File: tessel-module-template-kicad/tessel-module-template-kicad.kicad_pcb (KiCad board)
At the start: 2 copper layers, 0 parts

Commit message: added board outline and guides (we like our modules to be 1.1" high and (1+k*0.25)" long)
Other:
- board outline added: 25.4 x 27.9 mm
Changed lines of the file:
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@@
     (area 0 0 0 0)
     (thickness 1.6)
-    (drawings 0)
+    (drawings 14)
     (tracks 0)
     (zones 0)
@@
     (uvia_drill 0.1)
   )
+  (gr_line (start 171.45 127) (end 171.45 128.27) (layer Dwgs.User) (width 0.2))
+  (gr_line (start 158.75 127) (end 158.75 128.27) (layer Dwgs.User) (width 0.2))
+  (gr_line (start 152.4 127) (end 152.4 128.27) (layer Dwgs.User) (width 0.2))
+  (gr_line (start 165.1 127) (end 165.1 128.27) (layer Dwgs.User) (width 0.2))
+  (gr_line (start 146.05 127) (end 146.05 128.27) (layer Dwgs.User) (width 0.2))
+  (gr_line (start 139.7 127) (end 139.7 128.27) (layer Dwgs.User) (width 0.2))
+  (gr_line (start 133.35 127) (end 133.35 128.27) (layer Dwgs.User) (width 0.2))
+  (gr_line (start 127 127) (end 127 128.27) (layer Dwgs.User) (width 0.2))
+  (gr_arc (start 124.46 101.6) (end 124.46 99.06) (angle 90) (layer Edge.Cuts) (width 0.15))
+  (gr_arc (start 124.46 124.46) (end 127 124.46) (angle 90) (layer Edge.Cuts) (width 0.15))
+  (gr_line (start 124.46 127) (end 101.6 127) (layer Edge.Cuts) (width 0.15))
+  (gr_line (start 127 101.6) (end 127 124.46) (layer Edge.Cuts) (width 0.15))
+  (gr_line (start 101.6 99.06) (end 124.46 99.06) (layer Edge.Cuts) (width 0.15))
+  (gr_line (start 101.6 127) (end 101.6 99.06) (layer Edge.Cuts) (width 0.15))
 )

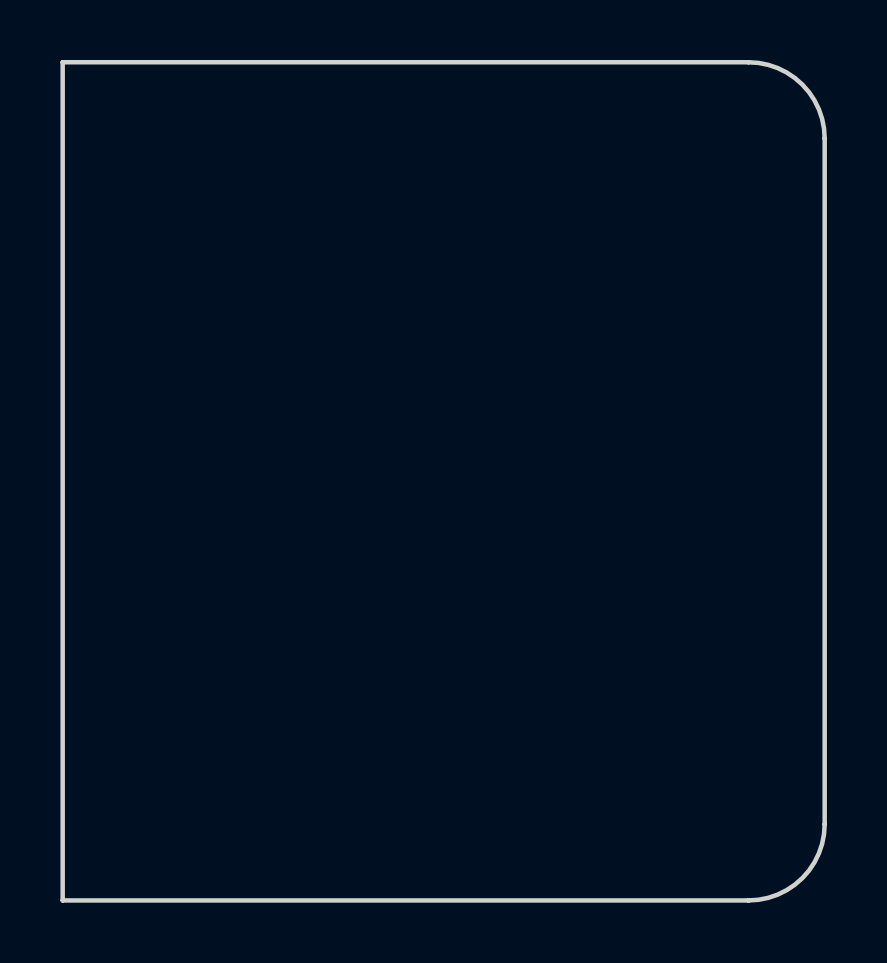
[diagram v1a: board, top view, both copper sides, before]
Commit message: read the netlist and placed the module header (centered on the vertical axis and in 75 mils on the horizontal axis). resized header refdes to 0.7mm text with 0.07mm width.
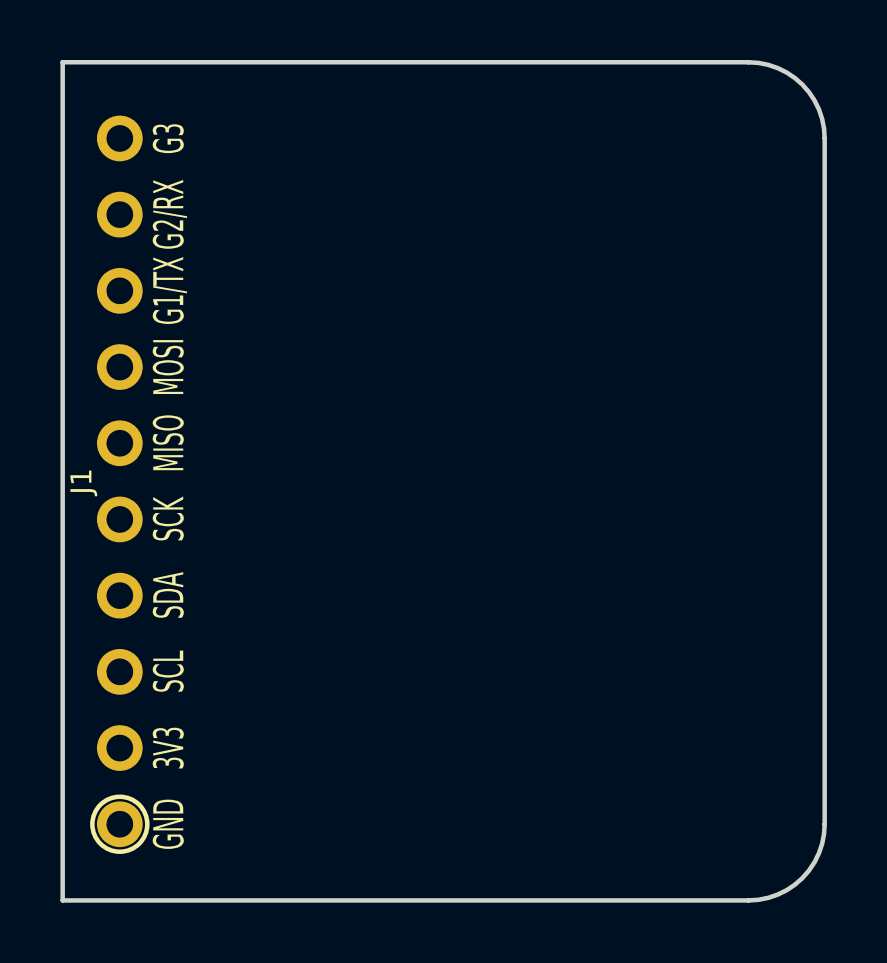
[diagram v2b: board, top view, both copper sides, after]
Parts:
- added J1: MODULE_HEADER, tm-kicad-lib:MODULE_HEADER_MODULE, F.Cu at (103.5, 113.0)
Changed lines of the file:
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@@
     (links 0)
     (no_connects 0)
-    (area 0 0 0 0)
+    (area 101.524999 98.984999 127.075001 127.075001)
     (thickness 1.6)
     (drawings 14)
     (tracks 0)
     (zones 0)
-    (modules 0)
-    (nets 1)
+    (modules 1)
+    (nets 11)
   )
   (page A4)
@@
   )
   (net 0 "")
+  (net 1 GND)
+  (net 2 +3V3)
+  (net 3 "Net-(J1-Pad3)")
+  (net 4 "Net-(J1-Pad4)")
+  (net 5 "Net-(J1-Pad5)")
+  (net 6 "Net-(J1-Pad6)")
+  (net 7 "Net-(J1-Pad7)")
+  (net 8 "Net-(J1-Pad8)")
+  (net 9 "Net-(J1-Pad9)")
+  (net 10 "Net-(J1-Pad10)")
   (net_class Default "This is the default net class."
     (clearance 0.2032)
@@
     (uvia_dia 0.3)
     (uvia_drill 0.1)
+    (add_net +3V3)
+    (add_net GND)
+    (add_net "Net-(J1-Pad10)")
+    (add_net "Net-(J1-Pad3)")
+    (add_net "Net-(J1-Pad4)")
+    (add_net "Net-(J1-Pad5)")
+    (add_net "Net-(J1-Pad6)")
+    (add_net "Net-(J1-Pad7)")
+    (add_net "Net-(J1-Pad8)")
+    (add_net "Net-(J1-Pad9)")
+  )
+  (module tm-kicad-lib:MODULE_HEADER_MODULE (layer F.Cu)
+    (at 103.505 113.03 90)
+    (fp_text reference J1 (at 0 -1.27 90) (layer F.SilkS)
+      (effects (font (size 0.7 0.7) (thickness 0.07)))
+    )
+    (fp_text value MODULE_HEADER (at -13.97 0 90) (layer F.SilkS) hide
+      (effects (font (size 1 1) (thickness 0.1)))
+    )
+    (fp_circle (center -11.43 0) (end -10.668 -0.508) (layer B.SilkS) (width 0.15))
+    (fp_circle (center -11.43 0) (end -10.668 -0.508) (layer F.SilkS) (width 0.15))
+    (fp_text user G3 (at 11.43 1.651 90) (layer F.SilkS)
+      (effects (font (size 1 0.55) (thickness 0.1)))
+    )
+    (fp_text user G2/RX (at 8.89 1.651 90) (layer F.SilkS)
+      (effects (font (size 1 0.55) (thickness 0.1)))
+    )
+    (fp_text user G1/TX (at 6.35 1.651 90) (layer F.SilkS)
+      (effects (font (size 1 0.55) (thickness 0.1)))
+    )
+    (fp_text user MOSI (at 3.81 1.651 90) (layer F.SilkS)
+      (effects (font (size 1 0.55) (thickness 0.1)))
+    )
+    (fp_text user MISO (at 1.27 1.651 90) (layer F.SilkS)
+      (effects (font (size 1 0.55) (thickness 0.1)))
+    )
+    (fp_text user SCK (at -1.27 1.651 90) (layer F.SilkS)
+      (effects (font (size 1 0.55) (thickness 0.1)))
+    )
+    (fp_text user SDA (at -3.81 1.651 90) (layer F.SilkS)
+      (effects (font (size 1 0.55) (thickness 0.1)))
+    )
+    (fp_text user SCL (at -6.35 1.651 90) (layer F.SilkS)
+      (effects (font (size 1 0.55) (thickness 0.1)))
+    )
+    (fp_text user 3V3 (at -8.89 1.651 90) (layer F.SilkS)
+      (effects (font (size 1 0.55) (thickness 0.1)))
+    )
+    (fp_text user GND (at -11.43 1.651 90) (layer F.SilkS)
+      (effects (font (size 1 0.55) (thickness 0.1)))
+    )
+    (pad 1 thru_hole circle (at -11.43 0 90) (size 1.524 1.524) (drill 0.889) (layers *.Cu *.Mask F.SilkS)
+      (net 1 GND))
+    (pad 2 thru_hole circle (at -8.89 0 90) (size 1.524 1.524) (drill 0.889) (layers *.Cu *.Mask F.SilkS)
+      (net 2 +3V3))
+    (pad 3 thru_hole circle (at -6.35 0 90) (size 1.524 1.524) (drill 0.889) (layers *.Cu *.Mask F.SilkS)
+      (net 3 "Net-(J1-Pad3)"))
+    (pad 4 thru_hole circle (at -3.81 0 90) (size 1.524 1.524) (drill 0.889) (layers *.Cu *.Mask F.SilkS)
+      (net 4 "Net-(J1-Pad4)"))
+    (pad 5 thru_hole circle (at -1.27 0 90) (size 1.524 1.524) (drill 0.889) (layers *.Cu *.Mask F.SilkS)
+      (net 5 "Net-(J1-Pad5)"))
+    (pad 6 thru_hole circle (at 1.27 0 90) (size 1.524 1.524) (drill 0.889) (layers *.Cu *.Mask F.SilkS)
+      (net 6 "Net-(J1-Pad6)"))
+    (pad 7 thru_hole circle (at 3.81 0 90) (size 1.524 1.524) (drill 0.889) (layers *.Cu *.Mask F.SilkS)
+      (net 7 "Net-(J1-Pad7)"))
+    (pad 8 thru_hole circle (at 6.35 0 90) (size 1.524 1.524) (drill 0.889) (layers *.Cu *.Mask F.SilkS)
+      (net 8 "Net-(J1-Pad8)"))
+    (pad 9 thru_hole circle (at 8.89 0 90) (size 1.524 1.524) (drill 0.889) (layers *.Cu *.Mask F.SilkS)
+      (net 9 "Net-(J1-Pad9)"))
+    (pad 10 thru_hole circle (at 11.43 0 90) (size 1.524 1.524) (drill 0.889) (layers *.Cu *.Mask F.SilkS)
+      (net 10 "Net-(J1-Pad10)"))
   )
   (gr_line (start 171.45 127) (end 171.45 128.27) (layer Dwgs.User) (width 0.2))
